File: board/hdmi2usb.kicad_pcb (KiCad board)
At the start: 2 copper layers, 177.8 x 106.7 mm, 301 parts, among them J1 USB_MICRO_B, J2 HDMI, J3 HDMI, J4 HDMI, J5 DVI-STACKED, J6 DVI-STACKED, J7 HDMI, J8 VHDCI, J9 DVI-STACKED, P1 CONN_7X2, U1 CY7C68013A, U10 LMR10530, U11 LMR10530, U12 LMR10530, U13 LP2997, U2 M25P16, U3 MT47H64M16HR, U4 IP4776CZ38, U5 IP4776CZ38, U6 IP4776CZ38, U7 IP4776CZ38, U8 SPARTAN6LXXXX-CSG324, U9 FXO-HC536R, X1 CRYSTAL

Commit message: Issue #510
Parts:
- removed R174, R175: R, SM0603
- removed R176: 50R, SM0603
- added C100, C101, C102, C103, C104, C105, C106, C107, C108, C110, C98, C99: 0.1mfd, SM0603, F.Cu at (304.9, 213.4)
- added C109: 15pf, SM0603, F.Cu at (304.9, 213.4)
- added L1, L2, L3: INDUCTOR, SM0805, F.Cu at (304.9, 213.4)
- C13, C14, C15, C16, C17, C18, C19, C20, C21, C22, C23, C24, C25: value 0.1MFD -> C
- C31, C32, C33, C34: value C -> 0.1MFD
- C35, C36, C37, C38, C39, C40, C41, C42, C43: value 0.1mfd -> 0.1MFD
- C44, C45, C46, C47: value 0.1mfd -> C
- C96: value 15pf -> 0.1mfd
- R100, R82, R84: value 50R -> 15K
- R101, R102: value 50R -> R
- R103: value 15K -> R
- R144, R145, R146: value R -> 0R
- R160, R161, R162: value 0R -> R
- R173: value R -> 50R
- R35, R36: value 20K -> R
- R37, R39, R41, R43: value 49.9R -> R
- R38: value 100R -> R
- R40, R42: value 4.7K -> R
- R44: value 49.9R -> 20K
- R45: value 100R -> 20K
- R46, R50: value 49.9R -> 100R
- R47, R49: value 49.9R -> 4.7K
- R48: footprint SM0603 -> RES_NET4
- R51, R52, R54: footprint SM0603 -> RES_NET4; moved to B.Cu
- R53: footprint SM0603 -> SM1206
- R57: value 49.9R -> 100K
- R58: value 49.9R -> 50R
- R59: value 49.9R -> 47K
- R60: value 100K -> 50R
- R61, R67, R91, R92: value 50R -> 47K
- R62, R64, R95: value 47K -> 50R
- R63, R65, R90: value 50R -> 100K
- R66, R68: value 100K -> 47K
- R70, R71, R72, R94: value 47K -> 1.5K
- R73, R77, R96: value 1.5K -> 27K
- R76: value 27K -> 1.5K
- R78: value 1.5K -> 15K
- R79, R97: value 1.5K -> 50R
- R81, R85, R87: value 15K -> 50R
- R83, R99: value 27K -> 50R
- R93: value 100K -> 1.5K
- U10, U11: value LMR10530 -> IP4776CZ38; footprint WFDN10 -> SSOP38
- U12: value LMR10530 -> SPARTAN6LXXXX-CSG324; footprint WFDN10 -> CSG324
- U13: value LP2997 -> FXO-HC536R; footprint SO8 -> FXO-HC536R
- U3: value MT47H64M16HR -> LMR10530; footprint BGA84 -> WFDN10
- U4, U5: value IP4776CZ38 -> LMR10530; footprint SSOP38 -> WFDN10
- U6: value IP4776CZ38 -> LP2997; footprint SSOP38 -> WFDN10
- U7: value IP4776CZ38 -> MT47H64M16HR; footprint SSOP38 -> BGA84
- U8: value SPARTAN6LXXXX-CSG324 -> IP4776CZ38; footprint CSG324 -> SSOP38
- U9: value FXO-HC536R -> IP4776CZ38; footprint FXO-HC536R -> SSOP38
- moved R51 277.5 mm to (194.8, 146.3)
- moved R54 271.9 mm to (189.7, 153.2), turned to 180 degrees
- moved R52 268.3 mm to (189.6, 146.4)
- moved U11 121.9 mm to (259.5, 188.1)
- moved U10 108.3 mm to (246.9, 188.7)
- moved U7 88.2 mm to (198.5, 157.2), turned to 180 degrees
- moved U12 75.8 mm to (232.0, 156.6)
- moved U8 72.3 mm to (168.3, 181.1)
- moved U9 60.0 mm to (177.5, 180.1), turned to 270 degrees
- moved U2 44.5 mm to (251.7, 118.0)
- moved C73 8.81 mm to (215.1, 138.9)
- moved C79 8.81 mm to (215.1, 134.9)
- moved C82 8.81 mm to (219.2, 134.9)
- moved C88 8.81 mm to (219.2, 138.9)
- moved C76 8.81 mm to (215.1, 136.9)
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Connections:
- C13 pad 1: N-00000250 -> /power/VCC5V0
- C14 pad 1: DDR0V9 -> /power/VCC5V0
- C15 pad 1: /MT47H64M16HR/VDD-1V8 -> /power/VCC5V0
- C16 pad 1: /MT47H64M16HR/VDDQ-1V8 -> N-00000258
- C17 pad 1: /MT47H64M16HR/VDD-1V8 -> N-00000269
- C18 pad 1: /MT47H64M16HR/VDDQ-1V8 -> N-00000266
- C19 pad 1: /MT47H64M16HR/VDD-1V8 -> /power/VCC3V3
- C20 pad 1: /MT47H64M16HR/VDDQ-1V8 -> /power/VCC1V2
- C21 pad 1: /MT47H64M16HR/VDD-1V8 -> /power/DDR1V8
- C22 pad 1: /MT47H64M16HR/VDDQ-1V8 -> /power/DDR1V8
- C23 pad 1: /MT47H64M16HR/VDD-1V8 -> /power/VCC5V0
- C24 pad 1: /MT47H64M16HR/VDDQ-1V8 -> N-00000264
- C25 pad 1: /MT47H64M16HR/VDD-1V8 -> /power/DDR0V9
- C26 pad 1: /MT47H64M16HR/VDDQ-1V8 -> N-00000253
- C27 pad 1: /MT47H64M16HR/VDDQ-1V8 -> DDR0V9
- C28 pad 1: /MT47H64M16HR/VDDQ-1V8 -> DDR1V8
- C29 pad 1: /MT47H64M16HR/VDDQ-1V8 -> DDR1V8
- C30 pad 1: /MT47H64M16HR/VDDQ-1V8 -> DDR1V8
- C31 pad 1: N-00000306 -> DDR1V8
- C32 pad 1: N-00000325 -> DDR1V8
- C33 pad 1: N-00000339 -> DDR1V8
- C34 pad 1: N-00000314 -> DDR1V8
- C35 pad 1: /spartan6/VCC3V3 -> DDR1V8
- C36 pad 1: VCC1V2 -> DDR1V8
- C37 pad 1: /spartan6/VCC3V3 -> DDR1V8
- C38 pad 1: /spartan6/VCC3V3 -> DDR1V8
- C39 pad 1: VCC1V2 -> DDR1V8
- C40 pad 1: /spartan6/VCC3V3 -> DDR1V8
- C41 pad 1: /spartan6/VCC3V3 -> DDR1V8
- C42 pad 1: VCC1V2 -> DDR1V8
- C43 pad 1: /spartan6/VCC3V3 -> DDR1V8
- C44 pad 1: /spartan6/VCC3V3 -> N-00000300
- C45 pad 1: VCC1V2 -> N-00000297
- C46 pad 1: /spartan6/VCC3V3 -> N-00000287
- C47 pad 1: /spartan6/VCC3V3 -> N-00000318
- C48 pad 1: VCC1V2 -> /spartan6/VCC3V3
- C49 pad 1: /spartan6/VCC3V3 -> VCC1V2
- C51 pad 1: VCC1V2 -> /spartan6/VCC3V3
- C52 pad 1: /spartan6/VCC3V3 -> VCC1V2
- C54 pad 1: VCC1V2 -> /spartan6/VCC3V3
- C55 pad 1: /spartan6/VCC3V3 -> VCC1V2
- C57 pad 1: VCC1V2 -> /spartan6/VCC3V3
- C58 pad 1: /spartan6/VCC3V3 -> VCC1V2
- C60 pad 1: VCC1V2 -> /spartan6/VCC3V3
- C61 pad 1: /spartan6/VCC3V3 -> VCC1V2
- C63 pad 1: VCC1V2 -> /spartan6/VCC3V3
- C64 pad 1: /spartan6/VCC3V3 -> VCC1V2
- C66 pad 1: VCC1V2 -> /spartan6/VCC3V3
- C67 pad 1: /spartan6/VCC3V3 -> VCC1V2
- C69 pad 1: VCC1V2 -> /spartan6/VCC3V3
- C70 pad 1: /spartan6/VCC3V3 -> VCC1V2
- C71 pad 1: VCC1V2 -> /spartan6/VCC3V3
- C73 pad 1: DDR1V8 -> VCC1V2
- C74 pad 1: VCC1V2 -> /spartan6/VCC3V3
- C76 pad 1: DDR1V8 -> VCC1V2
- C77 pad 1: VCC1V2 -> /spartan6/VCC3V3
- C79 pad 1: DDR1V8 -> VCC1V2
- C80 pad 1: VCC1V2 -> /spartan6/VCC3V3
- C82 pad 1: DDR1V8 -> VCC1V2
- C83 pad 1: VCC1V2 -> /spartan6/VCC3V3
- C84 pad 1: /spartan6/VCC3V3 -> VCC1V2
- C85 pad 1: DDR1V8 -> /spartan6/VCC3V3
- C86 pad 1: VCC1V2 -> DDR1V8
- C87 pad 1: /spartan6/VCC3V3 -> VCC1V2
- C88 pad 1: DDR1V8 -> /spartan6/VCC3V3
- C89 pad 1: VCC1V2 -> DDR1V8
- C90 pad 1: /spartan6/VCC3V3 -> VCC1V2
- C91 pad 1: VCC1V2 -> /spartan6/VCC3V3
- C92 pad 1: /spartan6/VCC3V3 -> DDR1V8
- C95 pad 1: /spartan6/VCC3V3 -> DDR1V8
- C96 pad 1: /spartan6/GCLK -> VCC1V2
- J8 pad 1: N-00000420 -> N-00000392
- J8 pad 10: N-00000416 -> N-00000388
- J8 pad 12: N-00000414 -> N-00000386
- J8 pad 13: N-00000412 -> N-00000384
- J8 pad 15: N-00000413 -> N-00000385
- J8 pad 20: N-00000411 -> N-00000383
- J8 pad 22: N-00000410 -> N-00000382
- J8 pad 23: N-00000409 -> N-00000381
- J8 pad 25: N-00000407 -> N-00000398
- J8 pad 26: N-00000408 -> N-00000397
- J8 pad 28: N-00000406 -> N-00000396
- J8 pad 29: N-00000423 -> N-00000379
- J8 pad 3: N-00000419 -> N-00000380
- J8 pad 31: N-00000422 -> N-00000395
- J8 pad 32: N-00000421 -> N-00000393
- J8 pad 34: N-00000425 -> N-00000399
- J8 pad 35: N-00000424 -> N-00000414
- J8 pad 37: N-00000441 -> N-00000413
- J8 pad 38: N-00000440 -> N-00000412
- J8 pad 4: N-00000418 -> N-00000391
- J8 pad 40: N-00000439 -> N-00000411
- J8 pad 41: N-00000438 -> N-00000410
- J8 pad 43: N-00000437 -> N-00000409
- J8 pad 44: N-00000436 -> N-00000404
- J8 pad 46: N-00000435 -> N-00000400
- J8 pad 47: N-00000431 -> N-00000401
- J8 pad 49: N-00000443 -> N-00000416
- J8 pad 54: N-00000442 -> N-00000415
- J8 pad 56: N-00000427 -> N-00000402
- J8 pad 57: N-00000428 -> N-00000403
- J8 pad 59: N-00000429 -> N-00000405
- J8 pad 6: N-00000405 -> N-00000390
- J8 pad 60: N-00000430 -> N-00000406
- J8 pad 62: N-00000426 -> N-00000407
- J8 pad 63: N-00000432 -> N-00000408
- J8 pad 65: N-00000433 -> N-00000419
- J8 pad 66: N-00000434 -> N-00000418
- J8 pad 68: N-00000444 -> N-00000417
- J8 pad 7: N-00000417 -> N-00000389
- J8 pad 9: N-00000415 -> N-00000387
- P1 pad 4: N-00000398 -> N-00000377
- P1 pad 6: N-00000397 -> N-00000378
- P1 pad 8: N-00000396 -> N-00000371
- R100 pad 1: VCC3V3 -> GND
- R100 pad 2: /hdmi/TMDS-RX2-1_N -> /hdmi/P3-SDA
- R101 pad 1: VCC3V3 -> /expansion connectors/EXP-IO1_P
- R101 pad 2: /hdmi/TMDS-RX2-0_N -> N-00000392
- R102 pad 1: VCC3V3 -> /spartan6/EXP-IO2_N
- R102 pad 2: /hdmi/TMDS-RX2-CLK_N -> N-00000380
- R103 pad 1: GND -> N-00000391
- R103 pad 2: /hdmi/P3-SDA -> /expansion connectors/EXP-IO3_P
- R104 pad 1: /expansion connectors/EXP-IO1_P -> N-00000390
- R104 pad 2: N-00000420 -> /expansion connectors/EXP-IO4_P
- R105 pad 1: /spartan6/EXP-IO2_N -> N-00000389
- R105 pad 2: N-00000419 -> /expansion connectors/EXP-IO5_P
- R106 pad 1: N-00000418 -> /expansion connectors/EXP-IO6_P
- R106 pad 2: /expansion connectors/EXP-IO3_P -> N-00000387
- R107 pad 1: N-00000405 -> N-00000388
- R107 pad 2: /expansion connectors/EXP-IO4_P -> /expansion connectors/EXP-IO7_P
- R108 pad 1: N-00000417 -> N-00000386
- R108 pad 2: /expansion connectors/EXP-IO5_P -> /expansion connectors/EXP-IO8_P
- R109 pad 1: /expansion connectors/EXP-IO6_P -> N-00000384
- R109 pad 2: N-00000415 -> /expansion connectors/EXP-IO9_P
- R110 pad 1: N-00000416 -> N-00000385
- R110 pad 2: /expansion connectors/EXP-IO7_P -> /expansion connectors/EXP-IO10_P
- R111 pad 1: N-00000414 -> N-00000383
- R111 pad 2: /expansion connectors/EXP-IO8_P -> /expansion connectors/EXP-IO11_P
- R112 pad 1: N-00000412 -> /expansion connectors/EXP-IO12_P
- R112 pad 2: /expansion connectors/EXP-IO9_P -> N-00000382
- R113 pad 1: N-00000413 -> N-00000381
- R113 pad 2: /expansion connectors/EXP-IO10_P -> /expansion connectors/EXP-IO13_P
- R114 pad 1: N-00000411 -> N-00000398
- R114 pad 2: /expansion connectors/EXP-IO11_P -> /expansion connectors/EXP-IO14_P
- R115 pad 1: /expansion connectors/EXP-IO12_P -> N-00000397
- R115 pad 2: N-00000410 -> /expansion connectors/EXP-IO15_P
- R116 pad 1: N-00000409 -> /expansion connectors/EXP-IO16_P
- R116 pad 2: /expansion connectors/EXP-IO13_P -> N-00000396
- R117 pad 1: N-00000407 -> N-00000379
- R117 pad 2: /expansion connectors/EXP-IO14_P -> /expansion connectors/EXP-IO17_P
- R118 pad 1: N-00000408 -> N-00000395
- R118 pad 2: /expansion connectors/EXP-IO15_P -> /expansion connectors/EXP-IO18_P
- R119 pad 1: /expansion connectors/EXP-IO16_P -> N-00000393
- R119 pad 2: N-00000406 -> /expansion connectors/EXP-IO19_P
- R120 pad 1: N-00000423 -> N-00000399
- R120 pad 2: /expansion connectors/EXP-IO17_P -> /expansion connectors/EXP-IO20_P
- R121 pad 1: N-00000422 -> N-00000414
- R121 pad 2: /expansion connectors/EXP-IO18_P -> /expansion connectors/EXP-IO1_N
- R122 pad 1: N-00000421 -> N-00000413
- R122 pad 2: /expansion connectors/EXP-IO19_P -> /expansion connectors/EXP-IO2_N
- R123 pad 1: N-00000425 -> /expansion connectors/EXP-IO3_N
- R123 pad 2: /expansion connectors/EXP-IO20_P -> N-00000412
- R124 pad 1: N-00000424 -> /expansion connectors/EXP-IO4_N
- R124 pad 2: /expansion connectors/EXP-IO1_N -> N-00000411
- R125 pad 1: N-00000441 -> /expansion connectors/EXP-IO5_N
- R125 pad 2: /expansion connectors/EXP-IO2_N -> N-00000410
- R126 pad 1: /expansion connectors/EXP-IO3_N -> N-00000409
- R126 pad 2: N-00000440 -> /expansion connectors/EXP-IO6_N
- R127 pad 1: /expansion connectors/EXP-IO4_N -> /expansion connectors/EXP-IO7_N
- R127 pad 2: N-00000439 -> N-00000404
- R128 pad 1: /expansion connectors/EXP-IO5_N -> /expansion connectors/EXP-IO8_N
- R128 pad 2: N-00000438 -> N-00000400
- R129 pad 1: N-00000437 -> /expansion connectors/EXP-IO9_N
- R129 pad 2: /expansion connectors/EXP-IO6_N -> N-00000401
- R130 pad 1: /expansion connectors/EXP-IO7_N -> /expansion connectors/EXP-IO10_N
- R130 pad 2: N-00000436 -> N-00000416
- R131 pad 1: /expansion connectors/EXP-IO8_N -> /expansion connectors/EXP-IO11_N
- R131 pad 2: N-00000435 -> N-00000415
- R132 pad 1: /expansion connectors/EXP-IO9_N -> N-00000402
- R132 pad 2: N-00000431 -> /expansion connectors/EXP-IO12_N
- R133 pad 1: /expansion connectors/EXP-IO10_N -> /expansion connectors/EXP-IO13_N
- R133 pad 2: N-00000443 -> N-00000403
- R134 pad 1: /expansion connectors/EXP-IO11_N -> /expansion connectors/EXP-IO14_N
- R134 pad 2: N-00000442 -> N-00000405
- R135 pad 1: N-00000427 -> /expansion connectors/EXP-IO15_N
- R135 pad 2: /expansion connectors/EXP-IO12_N -> N-00000406
- R136 pad 1: /expansion connectors/EXP-IO13_N -> N-00000407
- R136 pad 2: N-00000428 -> /expansion connectors/EXP-IO16_N
- R137 pad 1: /expansion connectors/EXP-IO14_N -> /expansion connectors/EXP-IO17_N
- R137 pad 2: N-00000429 -> N-00000408
- R138 pad 1: /expansion connectors/EXP-IO15_N -> /expansion connectors/EXP-IO18_N
- R138 pad 2: N-00000430 -> N-00000419
- R139 pad 1: N-00000426 -> /expansion connectors/EXP-IO19_N
- R139 pad 2: /expansion connectors/EXP-IO16_N -> N-00000418
- R140 pad 1: /expansion connectors/EXP-IO17_N -> /expansion connectors/EXP-IO20_N
- R140 pad 2: N-00000432 -> N-00000417
- R141 pad 1: /expansion connectors/EXP-IO18_N -> N-00000377
- R141 pad 2: N-00000433 -> /expansion connectors/TMS
- R142 pad 1: /expansion connectors/EXP-IO19_N -> N-00000378
- R142 pad 2: N-00000434 -> /expansion connectors/TCK
- R143 pad 1: /expansion connectors/EXP-IO20_N -> N-00000371
- R143 pad 2: N-00000444 -> /expansion connectors/TDO-FPGA/TDO-JTAG
- R144 pad 1: N-00000398 -> /spartan6/VCC3V3--OR--GND
- R144 pad 2: /expansion connectors/TMS -> /spartan6/VCC3V3
- R145 pad 1: N-00000397 -> /spartan6/VCC3V3--OR--GND
- R145 pad 2: /expansion connectors/TCK -> GND
- R146 pad 1: N-00000396 -> /spartan6/GTP-TX-ECLK_N--OR--VCC3V3
- R146 pad 2: /expansion connectors/TDO-FPGA/TDO-JTAG -> /spartan6/VCC3V3
- R147 pad 1: /spartan6/VCC3V3--OR--GND -> /spartan6/GTP-TX-ECLK_N--OR--VCC3V3
- R147 pad 2: /spartan6/VCC3V3 -> /expansion connectors/GTP-TX-ECLK_N
- R148 pad 1: /spartan6/VCC3V3--OR--GND -> /spartan6/GTP-RX-CLK_P--OR--VCC3V3
- R148 pad 2: GND -> /spartan6/VCC3V3
- R149 pad 1: /spartan6/GTP-TX-ECLK_N--OR--VCC3V3 -> /spartan6/GTP-RX-CLK_P--OR--VCC3V3
- R149 pad 2: /spartan6/VCC3V3 -> /expansion connectors/GTP-RX-CLK_P
- R150 pad 1: /spartan6/GTP-TX-ECLK_N--OR--VCC3V3 -> /spartan6/GTP-RX-1_P--OR--VCC3V3
- R150 pad 2: /expansion connectors/GTP-TX-ECLK_N -> /spartan6/VCC3V3
- R151 pad 1: /spartan6/GTP-RX-CLK_P--OR--VCC3V3 -> /spartan6/GTP-RX-1_P--OR--VCC3V3
- R151 pad 2: /spartan6/VCC3V3 -> /expansion connectors/GTP-RX-1_P
- R152 pad 1: /spartan6/GTP-RX-CLK_P--OR--VCC3V3 -> /spartan6/GTP-RX-3_P--OR--VCC3V3
- R152 pad 2: /expansion connectors/GTP-RX-CLK_P -> /spartan6/VCC3V3
- R153 pad 1: /spartan6/GTP-RX-1_P--OR--VCC3V3 -> /spartan6/GTP-RX-3_P--OR--VCC3V3
- R153 pad 2: /spartan6/VCC3V3 -> /expansion connectors/GTP-RX-3_P
- R154 pad 1: /spartan6/GTP-RX-1_P--OR--VCC3V3 -> /spartan6/GTP_CAL
- R154 pad 2: /expansion connectors/GTP-RX-1_P -> /spartan6/VCC3V3
- R155 pad 1: /spartan6/GTP-RX-3_P--OR--VCC3V3 -> /spartan6/GTP_CAL
- R155 pad 2: /spartan6/VCC3V3 -> VCC1V2
- R156 pad 1: /spartan6/GTP-RX-3_P--OR--VCC3V3 -> /spartan6/GND--OR--VCC1V2
- R156 pad 2: /expansion connectors/GTP-RX-3_P -> GND
- R157 pad 1: /spartan6/GTP_CAL -> /spartan6/GND--OR--VCC1V2
- R157 pad 2: /spartan6/VCC3V3 -> VCC1V2
- R158 pad 1: /spartan6/GTP_CAL -> /spartan6/GTP-RX-0_P--OR--GND
- R158 pad 2: VCC1V2 -> GND
- R159 pad 1: /spartan6/GND--OR--VCC1V2 -> /spartan6/GTP-RX-0_P--OR--GND
- R159 pad 2: GND -> /expansion connectors/GTP-RX-0_P
- R160 pad 1: /spartan6/GND--OR--VCC1V2 -> N-00000178
- R160 pad 2: VCC1V2 -> GND
- R161 pad 1: /spartan6/GTP-RX-0_P--OR--GND -> N-00000177
- R162 pad 1: /spartan6/GTP-RX-0_P--OR--GND -> N-00000179
- R162 pad 2: /expansion connectors/GTP-RX-0_P -> GND
- R163 pad 1: N-00000178 -> N-00000184
- R164 pad 1: N-00000177 -> N-00000174
- R165 pad 1: N-00000179 -> N-00000187
- R166 pad 1: N-00000184 -> N-00000188
- R166 pad 2: GND -> /spartan6/VCC3V3
- R167 pad 1: N-00000174 -> N-00000180
- R168 pad 1: N-00000187 -> N-00000163
- R168 pad 2: GND -> /spartan6/VCC3V3
- R169 pad 1: N-00000188 -> N-00000185
- R169 pad 2: /spartan6/VCC3V3 -> GND
- R170 pad 1: N-00000180 -> N-00000182
- R171 pad 1: N-00000163 -> N-00000175
- R171 pad 2: /spartan6/VCC3V3 -> GND
- R172 pad 1: N-00000185 -> N-00000186
- R173 pad 1: N-00000182 -> /spartan6/GTP-REF
- R173 pad 2: GND -> /spartan6/GTP_CAL
- R35 pad 1: /MT47H64M16HR/VDD-1V8 -> /power/VCC5V0
- R35 pad 2: N-00000250 -> N-00000258
- R36 pad 1: GND -> /power/VCC5V0
- R36 pad 2: N-00000250 -> N-00000269
- R37 pad 1: DDR0V9 -> /power/VCC5V0
- R37 pad 2: /MT47H64M16HR/DDR-A12 -> N-00000266
- R38 pad 1: N-00000256 -> /power/VCC3V3
- R38 pad 2: GND -> N-00000259
- R39 pad 1: DDR0V9 -> N-00000259
- R39 pad 2: /MT47H64M16HR/DDR-A11 -> GND
- R40 pad 1: /MT47H64M16HR/DDR-ODT -> /power/VCC1V2
- R40 pad 2: GND -> N-00000273
- R41 pad 1: DDR0V9 -> N-00000273
- R41 pad 2: /MT47H64M16HR/DDR-A10 -> GND
- R42 pad 1: /MT47H64M16HR/DDR-CKE -> /power/DDR1V8
- R42 pad 2: GND -> N-00000268
- R43 pad 1: DDR0V9 -> N-00000268
- R43 pad 2: /MT47H64M16HR/DDR-A9 -> GND
- R44 pad 1: DDR0V9 -> DDR1V8
- R44 pad 2: /MT47H64M16HR/DDR-A8 -> N-00000253
- R45 pad 1: /MT47H64M16HR/DDR-CK_N -> GND
- R45 pad 2: /MT47H64M16HR/DDR-CK_P -> N-00000253
- R46 pad 1: DDR0V9 -> N-00000256
- R46 pad 2: /MT47H64M16HR/DDR-A7 -> GND
- R47 pad 1: DDR0V9 -> /MT47H64M16HR/DDR-ODT
- R47 pad 2: /MT47H64M16HR/DDR-A6 -> GND
- R48 pad 2: /MT47H64M16HR/DDR-A5 -> /MT47H64M16HR/DDR-A12
- R49 pad 1: DDR0V9 -> /MT47H64M16HR/DDR-CKE
- R49 pad 2: /MT47H64M16HR/DDR-A4 -> GND
- R50 pad 1: DDR0V9 -> /MT47H64M16HR/DDR-CK_N
- R50 pad 2: /MT47H64M16HR/DDR-A3 -> /MT47H64M16HR/DDR-CK_P
- R51 pad 2: /MT47H64M16HR/DDR-A2 -> /MT47H64M16HR/DDR-A8
- R52 pad 2: /MT47H64M16HR/DDR-A1 -> /MT47H64M16HR/DDR-A4
- R53 pad 1: /MT47H64M16HR/DDR-BA0 -> DDR0V9
- R53 pad 2: DDR0V9 -> /MT47H64M16HR/DDR-A0
- R54 pad 1: DDR0V9 -> /MT47H64M16HR/DDR-BA0
- R54 pad 2: /MT47H64M16HR/DDR-A0 -> DDR0V9
- R55 pad 1: /MT47H64M16HR/DDR-BA1 -> /MT47H64M16HR/DDR-CAS
- R56 pad 1: /MT47H64M16HR/DDR-BA2 -> /MT47H64M16HR/DDR-WE
- R57 pad 1: /MT47H64M16HR/DDR-RAS -> VCC3V3
- R57 pad 2: DDR0V9 -> /hdmi/TMDS-TX2-CEC
- R58 pad 1: /MT47H64M16HR/DDR-CAS -> /hdmi/TMDS-RX1-CLK_P
- R58 pad 2: DDR0V9 -> VCC3V3
- R59 pad 1: /MT47H64M16HR/DDR-WE -> VCC3V3
- R59 pad 2: DDR0V9 -> /hdmi/TMDS-TX2-SCL
- R60 pad 1: VCC3V3 -> /hdmi/TMDS-RX1-0_P
- R60 pad 2: /hdmi/TMDS-TX2-CEC -> VCC3V3
- R61 pad 1: /hdmi/TMDS-RX1-CLK_P -> (no net)
- R61 pad 2: VCC3V3 -> /hdmi/TMDS-TX2-SDA
- R62 pad 1: VCC3V3 -> /hdmi/TMDS-RX1-1_P
- R62 pad 2: /hdmi/TMDS-TX2-SCL -> VCC3V3
- R63 pad 1: /hdmi/TMDS-RX1-0_P -> VCC3V3
- R63 pad 2: VCC3V3 -> /hdmi/TMDS-TX1-CEC
- R64 pad 1: (no net) -> /hdmi/TMDS-RX1-2_P
- R64 pad 2: /hdmi/TMDS-TX2-SDA -> VCC3V3
- R65 pad 1: /hdmi/TMDS-RX1-1_P -> VCC3V3
- R65 pad 2: VCC3V3 -> /hdmi/TMDS-RX1-CEC
- R66 pad 2: /hdmi/TMDS-TX1-CEC -> /hdmi/TMDS-TX1-SCL
- R67 pad 1: /hdmi/TMDS-RX1-2_P -> VCC3V3
- R67 pad 2: VCC3V3 -> /hdmi/TMDS-RX1-SCL
- R68 pad 1: VCC3V3 -> (no net)
- R68 pad 2: /hdmi/TMDS-RX1-CEC -> /hdmi/TMDS-TX1-SDA
- R69 pad 2: /hdmi/TMDS-TX1-SCL -> /hdmi/TMDS-RX1-SDA
- R70 pad 1: VCC3V3 -> VCC5V0
- R70 pad 2: /hdmi/TMDS-RX1-SCL -> /hdmi/P4-SDA
- R71 pad 1: (no net) -> VCC5V0
- R71 pad 2: /hdmi/TMDS-TX1-SDA -> /hdmi/P4-SCL
- R72 pad 1: VCC3V3 -> VCC5V0
- R72 pad 2: /hdmi/TMDS-RX1-SDA -> /hdmi/P2-SDA
- R73 pad 1: VCC5V0 -> VCC3V3
- R73 pad 2: /hdmi/P4-SDA -> /hdmi/P4-CEC
- R74 pad 2: /hdmi/P4-SCL -> /hdmi/P2-SCL
- R75 pad 2: /hdmi/P2-SDA -> /hdmi/P1-SDA
- R76 pad 1: VCC3V3 -> VCC5V0
- R76 pad 2: /hdmi/P4-CEC -> /hdmi/P1-SCL
- R77 pad 1: VCC5V0 -> VCC3V3
- R77 pad 2: /hdmi/P2-SCL -> /hdmi/P2-CEC
- R78 pad 1: VCC5V0 -> GND
- R78 pad 2: /hdmi/P1-SDA -> /hdmi/P4-HOT
- R79 pad 1: VCC5V0 -> /hdmi/TMDS-RX1-CLK_N
- R79 pad 2: /hdmi/P1-SCL -> VCC3V3
- R80 pad 2: /hdmi/P2-CEC -> /hdmi/P1-CEC
- R81 pad 1: GND -> /hdmi/TMDS-RX1-0_N
- R81 pad 2: /hdmi/P4-HOT -> VCC3V3
- R82 pad 1: /hdmi/TMDS-RX1-CLK_N -> GND
- R82 pad 2: VCC3V3 -> /hdmi/P2-SDA
- R83 pad 1: VCC3V3 -> /hdmi/TMDS-RX1-1_N
- R83 pad 2: /hdmi/P1-CEC -> VCC3V3
- R84 pad 1: /hdmi/TMDS-RX1-0_N -> GND
- R84 pad 2: VCC3V3 -> /hdmi/P1-HOT
- R85 pad 1: GND -> /hdmi/TMDS-RX1-2_N
- R85 pad 2: /hdmi/P2-SDA -> VCC3V3
- R86 pad 1: /hdmi/TMDS-RX1-1_N -> /hdmi/TMDS-RX2-2_P
- R87 pad 1: GND -> /hdmi/TMDS-RX2-1_P
- R87 pad 2: /hdmi/P1-HOT -> VCC3V3
- R88 pad 1: /hdmi/TMDS-RX1-2_N -> /hdmi/TMDS-RX2-0_P
- R89 pad 1: /hdmi/TMDS-RX2-2_P -> /hdmi/TMDS-RX2-CLK_P
- R90 pad 1: /hdmi/TMDS-RX2-1_P -> VCC3V3
- R90 pad 2: VCC3V3 -> /hdmi/TMDS-RX2-CEC
- R91 pad 1: /hdmi/TMDS-RX2-0_P -> VCC3V3
- R91 pad 2: VCC3V3 -> /hdmi/TMDS-RX2-SCL
- R92 pad 1: /hdmi/TMDS-RX2-CLK_P -> (no net)
- R92 pad 2: VCC3V3 -> /hdmi/TMDS-RX2-SDA
- R93 pad 1: VCC3V3 -> VCC5V0
- R93 pad 2: /hdmi/TMDS-RX2-CEC -> /hdmi/P3-SDA
- R94 pad 1: VCC3V3 -> VCC5V0
- R94 pad 2: /hdmi/TMDS-RX2-SCL -> /hdmi/P3-SCL
- R95 pad 1: (no net) -> VCC3V3
- R95 pad 2: /hdmi/TMDS-RX2-SDA -> /hdmi/TMDS-RX2-2_N
- R96 pad 1: VCC5V0 -> VCC3V3
- R96 pad 2: /hdmi/P3-SDA -> /hdmi/P3-CEC
- R97 pad 1: VCC5V0 -> VCC3V3
- R97 pad 2: /hdmi/P3-SCL -> /hdmi/TMDS-RX2-1_N
- R98 pad 2: /hdmi/TMDS-RX2-2_N -> /hdmi/TMDS-RX2-0_N
- R99 pad 2: /hdmi/P3-CEC -> /hdmi/TMDS-RX2-CLK_N
- U10 pad 1: (no net) -> VCC5V0
- U10 pad 10: (no net) -> /hdmi/TMDS-RX1-0_P
- U10 pad 2: (no net) -> VCC3V3
- U10 pad 3: (no net) -> GND
- U10 pad 4: (no net) -> /hdmi/TMDS-RX1-2_P
- U10 pad 5: (no net) -> GND
- U10 pad 7: (no net) -> /hdmi/TMDS-RX1-1_P
- U10 pad 8: (no net) -> GND
- U11 pad 1: (no net) -> VCC5V0
- U11 pad 10: (no net) -> /hdmi/TMDS-RX2-0_P
- U11 pad 2: (no net) -> VCC3V3
- U11 pad 3: (no net) -> GND
- U11 pad 4: (no net) -> /hdmi/TMDS-RX2-2_P
- U11 pad 5: (no net) -> GND
- U11 pad 7: (no net) -> /hdmi/TMDS-RX2-1_P
- U11 pad 8: (no net) -> GND
- U13 pad 1: (no net) -> /spartan6/VCC3V3
- U13 pad 2: (no net) -> GND
- U13 pad 3: (no net) -> /spartan6/GCLK
- U13 pad 4: (no net) -> /spartan6/VCC3V3
- U4 pad 1: VCC5V0 -> N-00000269
- U4 pad 10: /hdmi/TMDS-TX2-0_P -> /power/VCC5V0
- U4 pad 2: VCC3V3 -> N-00000269
- U4 pad 4: /hdmi/TMDS-TX2-2_P -> GND
- U4 pad 5: GND -> N-00000273
- U4 pad 6: (no net) -> GND
- U4 pad 7: /hdmi/TMDS-TX2-1_P -> N-00000272
- U4 pad 8: GND -> N-00000272
- U4 pad 9: (no net) -> /power/VCC5V0
- U5 pad 1: VCC5V0 -> N-00000266
- U5 pad 10: /hdmi/TMDS-TX1-0_P -> /power/VCC5V0
- U5 pad 2: VCC3V3 -> N-00000266
- U5 pad 4: /hdmi/TMDS-TX1-2_P -> GND
- U5 pad 5: GND -> N-00000268
- U5 pad 6: (no net) -> GND
- U5 pad 7: /hdmi/TMDS-TX1-1_P -> N-00000267
- U5 pad 8: GND -> N-00000267
- U5 pad 9: (no net) -> /power/VCC5V0
- U6 pad 1: VCC5V0 -> GND
- U6 pad 10: /hdmi/TMDS-RX1-0_P -> (no net)
- U6 pad 2: VCC3V3 -> /power/VCC5V0
- U6 pad 3: GND -> N-00000264
- U6 pad 4: /hdmi/TMDS-RX1-2_P -> (no net)
- U6 pad 5: GND -> /power/DDR1V8
- U6 pad 6: (no net) -> /power/VCC5V0
- U6 pad 7: /hdmi/TMDS-RX1-1_P -> /power/DDR1V8
- U6 pad 8: GND -> /power/DDR0V9
- U9 pad 1: /spartan6/VCC3V3 -> VCC5V0
- U9 pad 2: GND -> VCC3V3
- U9 pad 3: /spartan6/GCLK -> GND
- U9 pad 4: /spartan6/VCC3V3 -> /hdmi/TMDS-TX1-2_P
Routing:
- net /MT47H64M16HR/DDR-D8: track 0.00 -> 37.5 mm, vias 0 -> 2
- net /MT47H64M16HR/DDR-D15: track 0.00 -> 36.0 mm, vias 0 -> 2
- net /MT47H64M16HR/DDR-D13: track 0.00 -> 35.9 mm, vias 0 -> 2
- net /MT47H64M16HR/DDR-D7: track 0.00 -> 33.5 mm, vias 0 -> 2
- net /MT47H64M16HR/DDR-D5: track 0.00 -> 32.7 mm, vias 0 -> 2
- net /MT47H64M16HR/DDR-D0: track 0.00 -> 31.7 mm, vias 0 -> 2
- net /MT47H64M16HR/DDR-D2: track 0.00 -> 31.6 mm, vias 0 -> 2
- net /MT47H64M16HR/DDR-D10: track 0.00 -> 29.6 mm, vias 0 -> 2
- net /MT47H64M16HR/DDR-D6: track 0.00 -> 27.5 mm, vias 0 -> 2
- net /MT47H64M16HR/DDR-D3: track 0.00 -> 26.9 mm, vias 0 -> 2
- net /MT47H64M16HR/DDR-D9: track 0.00 -> 26.4 mm, vias 0 -> 2
- net /MT47H64M16HR/DDR-D11: track 0.00 -> 25.6 mm, vias 0 -> 2
- net /MT47H64M16HR/DDR-D1: track 0.00 -> 25.5 mm, vias 0 -> 2
- net /MT47H64M16HR/DDR-D14: track 0.00 -> 25.4 mm, vias 0 -> 2
- net /MT47H64M16HR/DDR-D12: track 0.00 -> 24.9 mm, vias 0 -> 2
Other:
- copper layers 2 -> 8
- net class Default: clearance 0.254 -> 0.1016; trace_width 0.254 -> 0.127; via_dia 0.889 -> 0.4572; via_drill 0.635 -> 0.254
- rule trace_clearance: 0.254 -> 0.1016
- rule trace_min: 0.254 -> 0.127
- rule via_min_drill: 0.508 -> 0.254
- rule via_min_size: 0.889 -> 0.4572

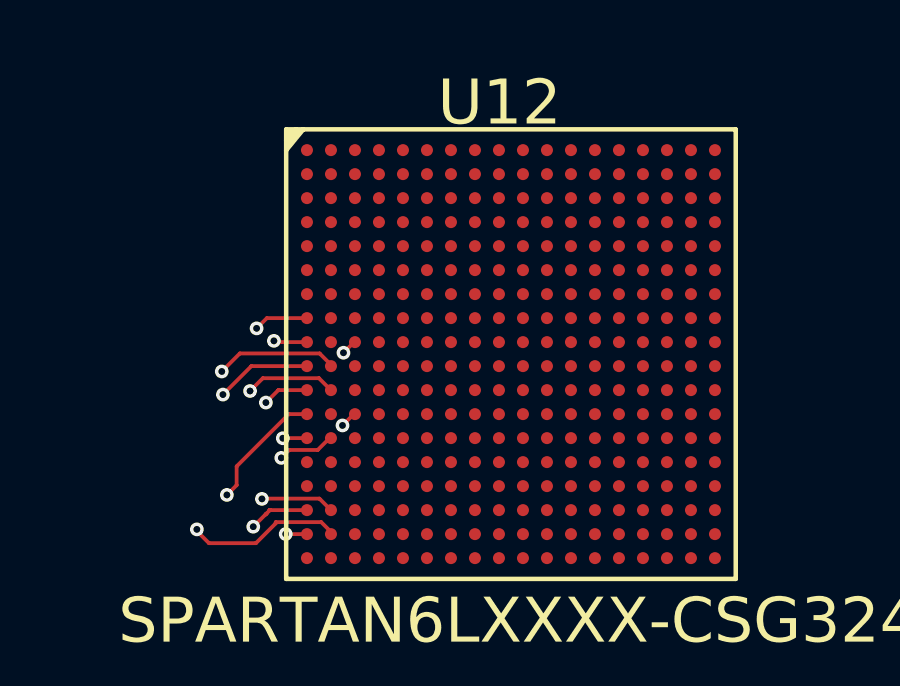
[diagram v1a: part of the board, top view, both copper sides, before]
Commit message: Issue #510 - Fanout of Spartan6
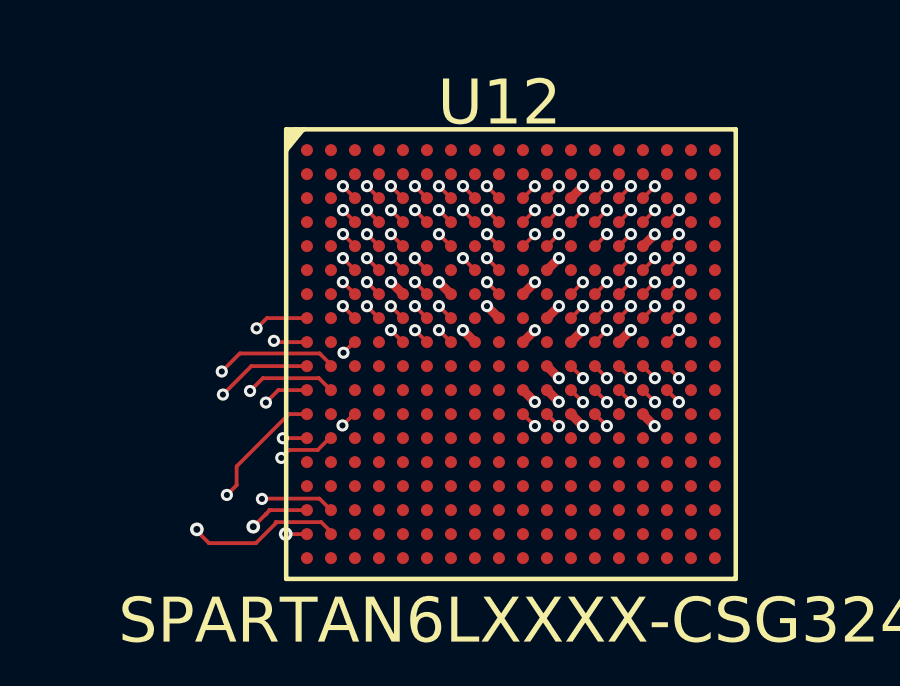
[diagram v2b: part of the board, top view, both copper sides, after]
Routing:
- net VCC1V2: track 0.00 -> 6.77 mm, vias 0 -> 12
- net /spartan6/VCC3V3: track 0.00 -> 3.96 mm, vias 0 -> 7
- net GND: track 0.00 -> 2.81 mm, vias 0 -> 5
- net DDR1V8: track 0.00 -> 1.13 mm, vias 0 -> 2
- net /spartan6/GTP_CAL: track 0.00 -> 1.13 mm, vias 0 -> 2
- net /spartan6/VCC3V3--OR--GND: track 0.00 -> 1.13 mm, vias 0 -> 2
- net /MT47H64M16HR/DDR-CK_P: track 0.00 -> 0.57 mm, vias 0 -> 1
- net /MT47H64M16HR/DDR-A6: track 0.00 -> 0.57 mm, vias 0 -> 1
- net /hdmi/TMDS-TX2-SCL: track 0.00 -> 0.57 mm, vias 0 -> 1
- net /spartan6/U1-SLOE: track 0.00 -> 0.57 mm, vias 0 -> 1
- net /MT47H64M16HR/DDR-A2: track 0.00 -> 0.57 mm, vias 0 -> 1
- net /expansion connectors/GTP-RX-ECLK_N: track 0.00 -> 0.57 mm, vias 0 -> 1
- net N-00000185: track 0.00 -> 0.57 mm, vias 0 -> 1
- net /expansion connectors/TDO-FPGA/TDO-JTAG: track 0.00 -> 0.57 mm, vias 0 -> 1
- net N-00000180: track 0.00 -> 0.57 mm, vias 0 -> 1
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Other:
- net class Default: via_dia 0.4572 -> 0.4064
- rule via_min_size: 0.4572 -> 0.4064

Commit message: Issue #510 - DDR routing
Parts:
- removed C27: 0.1MFD, SM0603_Capa
- removed FB1, FB2, FB3: FILTER, SM0805
- added R174: 49.9R, SM0603, B.Cu at (207.5, 155.0)
- added R175: 49.9R, SM0603, B.Cu at (192.0, 152.2)
- added R176: 49.9R, SM0603, B.Cu at (192.0, 153.9)
- R48, R49, R50, R55, R56: moved to B.Cu
- R51: footprint RES_NET4 -> SM0603
- R53: footprint SM1206 -> SM0603; moved to B.Cu
- moved R53 289.7 mm to (207.5, 153.5), turned to 180 degrees
- moved R56 283.3 mm to (192.0, 157.2), turned to 180 degrees
- moved R55 280.9 mm to (192.9, 155.5), turned to 180 degrees
- moved R49 279.0 mm to (204.4, 158.1)
- moved R50 274.6 mm to (198.7, 156.2), turned to 270 degrees
- moved R46 271.5 mm to (191.8, 154.5), turned to 180 degrees
- moved R48 264.0 mm to (195.8, 149.1)
- moved R44 252.2 mm to (204.8, 157.0), turned to 180 degrees
- moved R47 249.2 mm to (191.3, 156.4), turned to 180 degrees
- moved R45 244.3 mm to (204.9, 155.3), turned to 180 degrees
- moved C26 242.6 mm to (204.9, 153.5)
- moved R52 15.5 mm to (204.2, 151.7), turned to 270 degrees
- moved R54 14.7 mm to (204.3, 155.5), turned to 90 degrees
- moved R51 8.37 mm to (200.7, 140.3), turned to 180 degrees
- moved C109 6.54 mm to (311.4, 213.8)
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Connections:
- R48 pad 1: DDR0V9 -> /MT47H64M16HR/DDR-A4
- R48 pad 2: /MT47H64M16HR/DDR-A12 -> DDR0V9
- R48 pad 3: DDR0V9 -> /MT47H64M16HR/DDR-A6
- R48 pad 4: /MT47H64M16HR/DDR-A11 -> DDR0V9
- R48 pad 5: DDR0V9 -> /MT47H64M16HR/DDR-A8
- R48 pad 6: /MT47H64M16HR/DDR-A10 -> DDR0V9
- R48 pad 7: DDR0V9 -> /MT47H64M16HR/DDR-A11
- R48 pad 8: /MT47H64M16HR/DDR-A9 -> DDR0V9
- R51 pad 2: /MT47H64M16HR/DDR-A8 -> /MT47H64M16HR/DDR-A3
- R52 pad 1: DDR0V9 -> /MT47H64M16HR/DDR-A12
- R52 pad 2: /MT47H64M16HR/DDR-A4 -> DDR0V9
- R52 pad 3: DDR0V9 -> /MT47H64M16HR/DDR-A9
- R52 pad 4: /MT47H64M16HR/DDR-A3 -> DDR0V9
- R52 pad 5: DDR0V9 -> /MT47H64M16HR/DDR-A7
- R52 pad 6: /MT47H64M16HR/DDR-A2 -> DDR0V9
- R52 pad 7: DDR0V9 -> /MT47H64M16HR/DDR-A5
- R52 pad 8: /MT47H64M16HR/DDR-A1 -> DDR0V9
- R53 pad 2: /MT47H64M16HR/DDR-A0 -> /MT47H64M16HR/DDR-A10
- R54 pad 1: /MT47H64M16HR/DDR-BA0 -> DDR0V9
- R54 pad 2: DDR0V9 -> /MT47H64M16HR/DDR-WE
- R54 pad 3: /MT47H64M16HR/DDR-BA1 -> DDR0V9
- R54 pad 4: DDR0V9 -> /MT47H64M16HR/DDR-BA0
- R54 pad 5: /MT47H64M16HR/DDR-BA2 -> DDR0V9
- R54 pad 6: DDR0V9 -> /MT47H64M16HR/DDR-BA2
- R54 pad 7: /MT47H64M16HR/DDR-RAS -> DDR0V9
- R54 pad 8: DDR0V9 -> /MT47H64M16HR/DDR-BA1
- R56 pad 1: /MT47H64M16HR/DDR-WE -> /MT47H64M16HR/DDR-RAS
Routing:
- net /MT47H64M16HR/DDR-D8: track 37.5 -> 0.56 mm, vias 2 -> 1
- net /MT47H64M16HR/DDR-D5: track 32.7 -> 0.00 mm, vias 2 -> 0
- net GND: track 2.81 -> 11.9 mm, vias 5 -> 20
- net /MT47H64M16HR/DDR-D13: track 35.9 -> 30.8 mm
- net /spartan6/VCC3V3: track 3.96 -> 8.49 mm, vias 7 -> 15
- net /MT47H64M16HR/DDR-D15: track 36.0 -> 32.2 mm
- net /MT47H64M16HR/DDR-D9: track 26.4 -> 30.0 mm
- net /MT47H64M16HR/DDR-D7: track 33.5 -> 31.4 mm
- net /MT47H64M16HR/DDR-D2: track 31.6 -> 29.7 mm
- net VCC1V2: track 6.77 -> 8.45 mm, vias 12 -> 15
- net /MT47H64M16HR/DDR-D3: track 26.9 -> 25.4 mm
- net /spartan6/DDR0V9: track 0.00 -> 1.13 mm, vias 0 -> 2
- net /MT47H64M16HR/DDR-D1: track 25.5 -> 24.8 mm
- net /MT47H64M16HR/DDR-D6: track 27.5 -> 28.2 mm
- net /MT47H64M16HR/DDR-D10: track 29.6 -> 30.3 mm
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
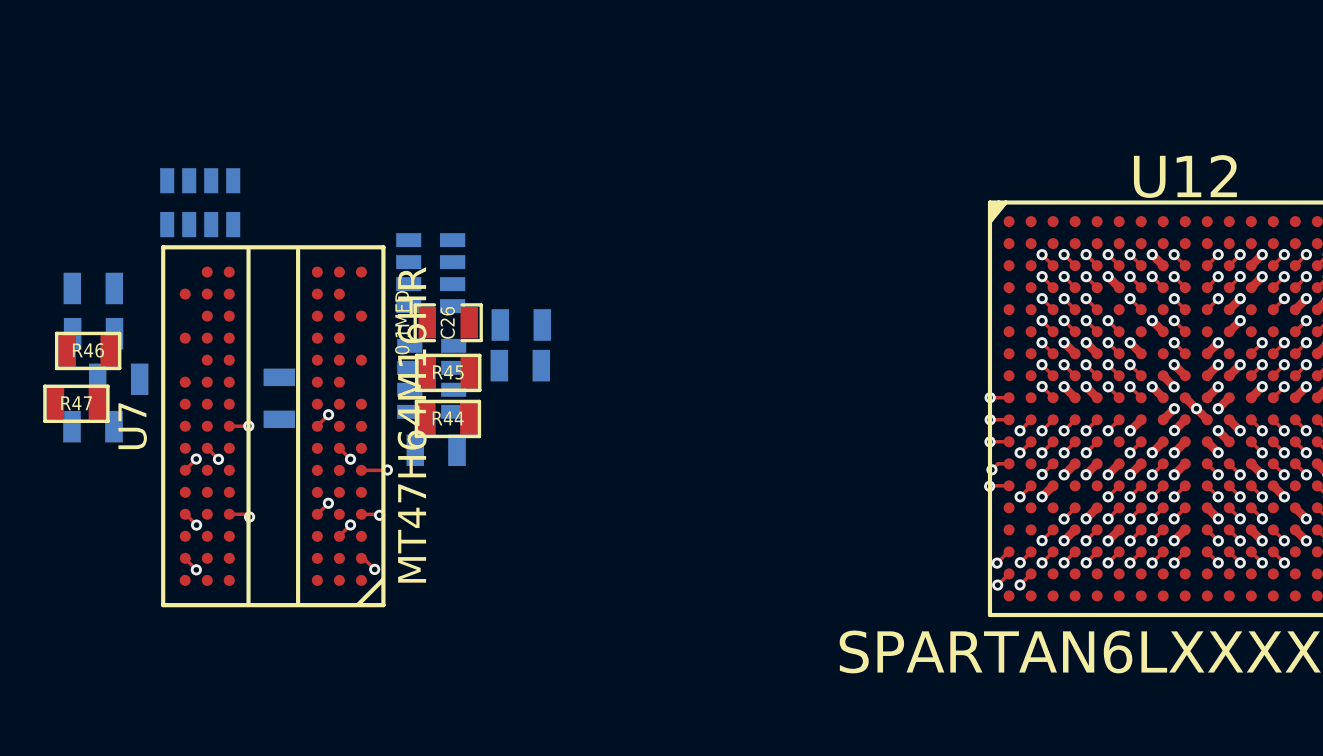
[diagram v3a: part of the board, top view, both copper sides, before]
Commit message: Issue #510 - DDR Routing dome by manu
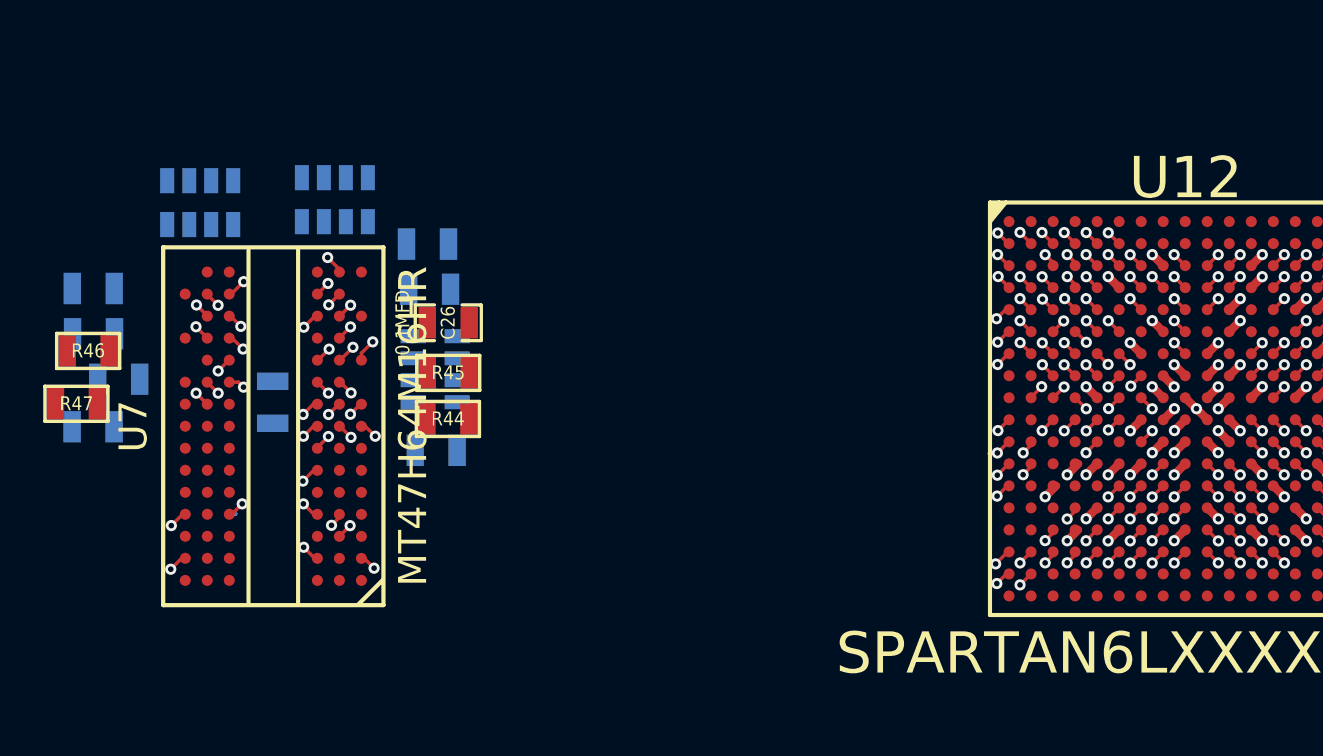
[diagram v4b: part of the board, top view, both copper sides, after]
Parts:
- moved R53 4.50 mm to (204.1, 150.6)
- moved R52 4.38 mm to (200.7, 149.0), turned to 180 degrees
- moved R174 4.31 mm to (204.2, 152.2)
- moved R54 0.37 mm to (204.4, 155.2)
- moved R50 0.28 mm to (198.5, 156.4)
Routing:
- net /MT47H64M16HR/DDR-A12: track 0.57 -> 50.8 mm, vias 1 -> 2
- net /MT47H64M16HR/DDR-A0: track 0.57 -> 48.7 mm, vias 1 -> 2
- net /MT47H64M16HR/DDR-A3: track 0.57 -> 43.3 mm, vias 1 -> 2
- net /MT47H64M16HR/DDR-A4: track 0.57 -> 37.9 mm, vias 1 -> 2
- net /MT47H64M16HR/DDR-CAS: track 0.57 -> 35.4 mm, vias 1 -> 2
- net /MT47H64M16HR/DDR-A7: track 0.57 -> 34.7 mm, vias 1 -> 2
- net /MT47H64M16HR/DDR-CK_P: track 0.57 -> 34.3 mm, vias 1 -> 2
- net /MT47H64M16HR/DDR-A2: track 0.57 -> 34.2 mm, vias 1 -> 2
- net /MT47H64M16HR/DDR-RAS: track 0.56 -> 34.0 mm, vias 1 -> 2
- net /MT47H64M16HR/DDR-A6: track 0.57 -> 33.3 mm, vias 1 -> 2
- net /MT47H64M16HR/DDR-A8: track 0.00 -> 32.1 mm, vias 0 -> 2
- net /MT47H64M16HR/DDR-A11: track 0.57 -> 32.3 mm, vias 1 -> 2
- net /MT47H64M16HR/DDR-D7: track 31.4 -> 0.00 mm, vias 2 -> 0
- net /MT47H64M16HR/DDR-UDM: track 0.57 -> 31.9 mm, vias 1 -> 2
- net /MT47H64M16HR/DDR-A5: track 0.57 -> 31.4 mm, vias 1 -> 2
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
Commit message: Issue #510
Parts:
- C28, C30, C32, C34, C36, C38, C86: moved to B.Cu
- moved C86 272.1 mm to (206.7, 131.6), turned to 180 degrees
- moved C32 253.0 mm to (171.8, 160.0)
- moved C30 250.4 mm to (176.1, 163.2), turned to 270 degrees
- moved C28 247.5 mm to (178.5, 163.3), turned to 90 degrees
- moved C34 235.9 mm to (171.7, 158.3)
- moved C36 209.0 mm to (174.5, 158.3), turned to 180 degrees
- moved C38 72.6 mm to (174.8, 160.5)
- moved R49 37.2 mm to (169.0, 146.6)
- moved C26 37.2 mm to (169.5, 142.0)
- moved R174 37.2 mm to (168.8, 140.8)
- moved R44 37.2 mm to (169.5, 145.5)
- moved R45 37.2 mm to (169.5, 143.8)
- moved R52 35.2 mm to (165.6, 150.3), turned to 90 degrees
- moved R53 32.2 mm to (175.3, 136.1)
- moved R48 30.8 mm to (165.6, 154.7), turned to 90 degrees
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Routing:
- net /MT47H64M16HR/DDR-A12: track 50.8 -> 1.17 mm
- net /MT47H64M16HR/DDR-A0: track 48.7 -> 1.15 mm
- net /MT47H64M16HR/DDR-A3: track 43.3 -> 1.17 mm
- net /MT47H64M16HR/DDR-A4: track 37.9 -> 1.08 mm
- net /MT47H64M16HR/DDR-CAS: track 35.4 -> 1.20 mm
- net /MT47H64M16HR/DDR-A7: track 34.7 -> 1.15 mm
- net /MT47H64M16HR/DDR-CK_P: track 34.3 -> 1.12 mm
- net /MT47H64M16HR/DDR-A2: track 34.2 -> 1.21 mm
- net /MT47H64M16HR/DDR-RAS: track 34.0 -> 1.21 mm
- net /MT47H64M16HR/DDR-A6: track 33.3 -> 1.18 mm
- net /MT47H64M16HR/DDR-A8: track 32.1 -> 0.55 mm, vias 2 -> 1
- net /MT47H64M16HR/DDR-A11: track 32.3 -> 1.23 mm
- net /MT47H64M16HR/DDR-UDM: track 31.9 -> 1.06 mm
- net /MT47H64M16HR/DDR-D13: track 32.2 -> 1.91 mm, vias 2 -> 1
- net /MT47H64M16HR/DDR-A5: track 31.4 -> 1.11 mm
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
